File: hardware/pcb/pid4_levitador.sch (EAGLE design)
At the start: 108 parts, among them P1_C1 1u, P1_C2 1u, P1_IC1 TL074CN, P1_IC2 TL074CN, P1_J_IN VSENSOR, P1_J_OUT VPID, P1_J_PWR PWR, P1_POT1 22k, P1_POT2 220k, P1_POT3 22k, P1_R1 10k, P1_R10 1k, P1_R11 1M, P1_R12 160k, P1_R13 240k, P1_R14 96k, P1_R15 160k, P1_R2 10k, P1_R3 10k, P1_R4 10k, P1_R5 10k, P1_R6 1k, P1_R7 10k, P1_R8 10k, P1_R9 10k, P1_RBIAS 4.4k, P1_ROFFSET 10k, P2_C1 1u, P2_C2 1u, P2_IC1 TL074CN, P2_IC2 TL074CN, P2_J_IN VSENSOR, P2_J_OUT VPID, P2_J_PWR PWR, P2_POT1 22k, P2_POT2 220k, P2_POT3 22k, P2_R1 10k, P2_R10 1k, P2_R11 1M, P2_R12 160k, P2_R13 240k, P2_R14 96k, P2_R15 160k, P2_R2 10k, P2_R3 10k, P2_R4 10k, P2_R5 10k, P2_R6 1k, P2_R7 10k, P2_R8 10k, P2_R9 10k, P2_RBIAS 4.4k, P2_ROFFSET 10k, P3_C1 1u, P3_C2 1u, P3_IC1 TL074CN, P3_IC2 TL074CN, P3_J_IN VSENSOR, P3_J_OUT VPID, P3_J_PWR PWR, P3_POT1 22k, P3_POT2 220k, P3_POT3 22k, P3_R1 10k, P3_R10 1k, P3_R11 1M, P3_R12 160k, P3_R13 240k, P3_R14 96k, P3_R15 160k, P3_R2 10k, P3_R3 10k, P3_R4 10k, P3_R5 10k, P3_R6 1k, P3_R7 10k, P3_R8 10k, P3_R9 10k, P3_RBIAS 4.4k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

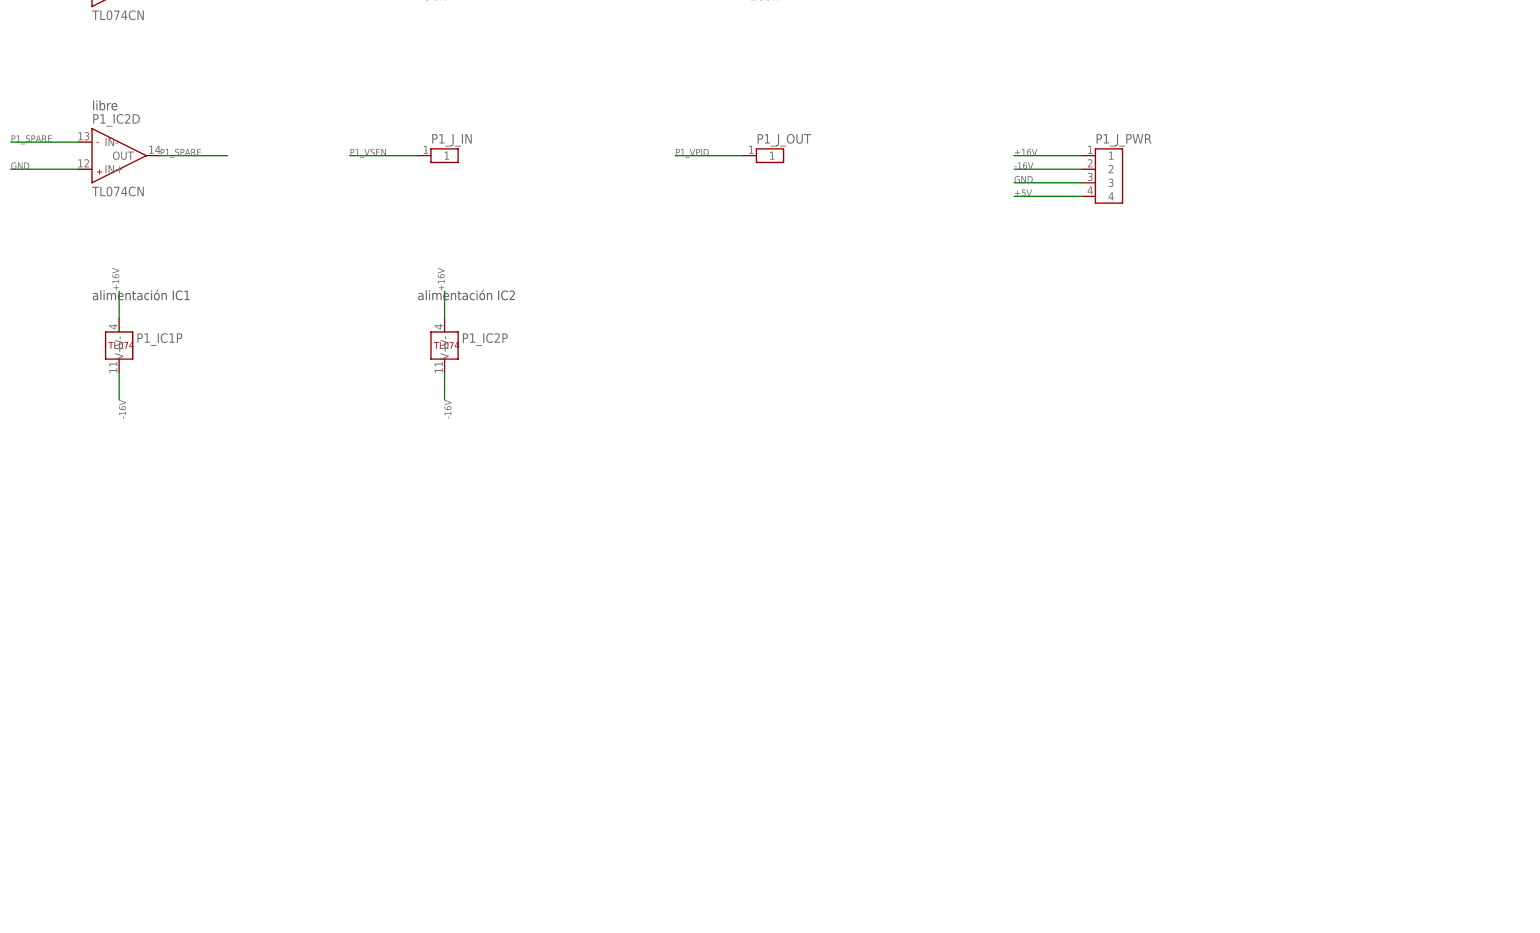
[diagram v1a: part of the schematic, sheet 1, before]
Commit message: Agrega la etapa de potencia a cada uno de los 4 PID de la placa (TIP122, banco de sensado 10 x 1R, protección y bornes de bobina)
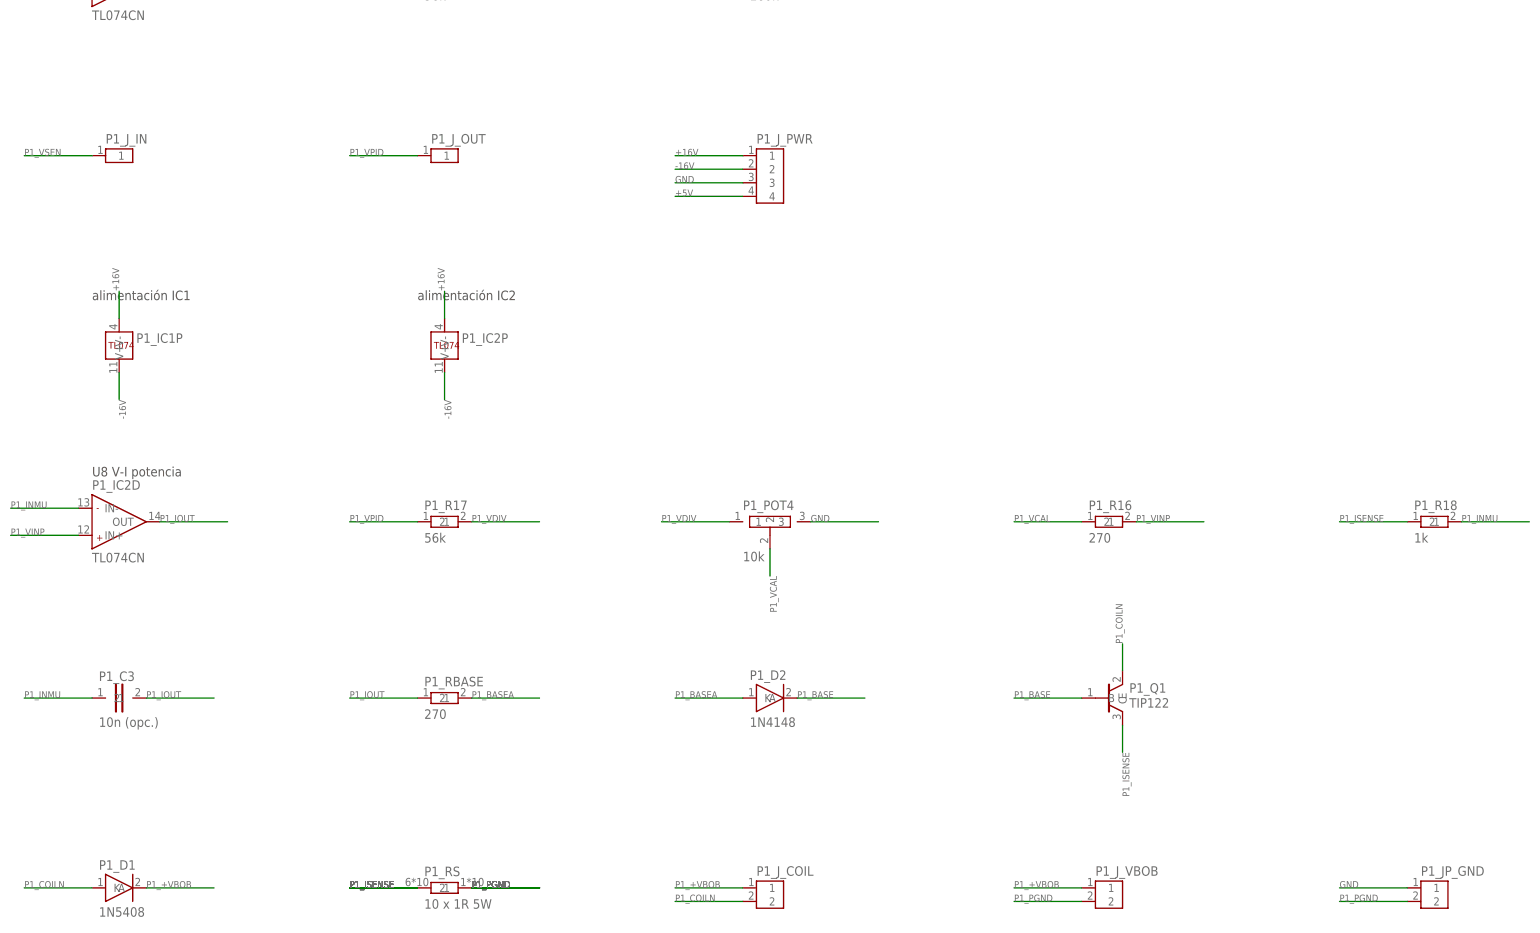
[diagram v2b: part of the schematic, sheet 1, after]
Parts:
- added P1_C3, P2_C3, P3_C3, P4_C3: 10n (opc.), pid4:C
- added P1_D1, P2_D1, P3_D1, P4_D1: 1N5408, pid4:D1N5408
- added P1_D2, P2_D2, P3_D2, P4_D2: 1N4148, pid4:D1N4148
- added P1_JP_GND, P2_JP_GND, P3_JP_GND, P4_JP_GND: GND-PGND, pid4:HDR2
- added P1_J_COIL, P2_J_COIL, P3_J_COIL, P4_J_COIL: BOBINA, pid4:TERM2
- added P1_J_VBOB, P2_J_VBOB, P3_J_VBOB, P4_J_VBOB: VBOB, pid4:TERM2
- added P1_POT4, P2_POT4, P3_POT4, P4_POT4: 10k, pid4:POT
- added P1_Q1, P2_Q1, P3_Q1, P4_Q1: TIP122, pid4:TIP122
- added P1_R16, P1_RBASE, P2_R16, P2_RBASE, P3_R16, P3_RBASE, P4_R16, P4_RBASE: 270, pid4:R
- added P1_R17, P2_R17, P3_R17, P4_R17: 56k, pid4:R
- added P1_R18, P2_R18, P3_R18, P4_R18: 1k, pid4:R
- added P1_RS, P2_RS, P3_RS, P4_RS: 10 x 1R 5W, pid4:RSB
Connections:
- removed net P1_SPARE: P1_IC2D.IN-, P1_IC2D.OUT
- removed net P2_SPARE: P2_IC2D.IN-, P2_IC2D.OUT
- removed net P3_SPARE: P3_IC2D.IN-, P3_IC2D.OUT
- removed net P4_SPARE: P4_IC2D.IN-, P4_IC2D.OUT
- new net P1_+VBOB: P1_D1.K, P1_J_COIL.1, P1_J_VBOB.1
- new net P1_BASE: P1_D2.K, P1_Q1.B
- new net P1_BASEA: P1_D2.A, P1_RBASE.2
- new net P1_COILN: P1_D1.A, P1_J_COIL.2, P1_Q1.C
- new net P1_INMU: P1_C3.1, P1_IC2D.IN-, P1_R18.2
- new net P1_IOUT: P1_C3.2, P1_IC2D.OUT, P1_RBASE.1
- new net P1_ISENSE: P1_Q1.E, P1_R18.1, P1_RS.1
- new net P1_PGND: P1_JP_GND.2, P1_J_VBOB.2, P1_RS.2
- new net P1_VCAL: P1_POT4.2, P1_R16.1
- new net P1_VDIV: P1_POT4.1, P1_R17.2
- new net P1_VINP: P1_IC2D.IN+, P1_R16.2
- new net P2_+VBOB: P2_D1.K, P2_J_COIL.1, P2_J_VBOB.1
- new net P2_BASE: P2_D2.K, P2_Q1.B
- new net P2_BASEA: P2_D2.A, P2_RBASE.2
- new net P2_COILN: P2_D1.A, P2_J_COIL.2, P2_Q1.C
- new net P2_INMU: P2_C3.1, P2_IC2D.IN-, P2_R18.2
- new net P2_IOUT: P2_C3.2, P2_IC2D.OUT, P2_RBASE.1
- new net P2_ISENSE: P2_Q1.E, P2_R18.1, P2_RS.1
- new net P2_PGND: P2_JP_GND.2, P2_J_VBOB.2, P2_RS.2
- new net P2_VCAL: P2_POT4.2, P2_R16.1
- new net P2_VDIV: P2_POT4.1, P2_R17.2
- new net P2_VINP: P2_IC2D.IN+, P2_R16.2
- new net P3_+VBOB: P3_D1.K, P3_J_COIL.1, P3_J_VBOB.1
- new net P3_BASE: P3_D2.K, P3_Q1.B
- new net P3_BASEA: P3_D2.A, P3_RBASE.2
- new net P3_COILN: P3_D1.A, P3_J_COIL.2, P3_Q1.C
- new net P3_INMU: P3_C3.1, P3_IC2D.IN-, P3_R18.2
- new net P3_IOUT: P3_C3.2, P3_IC2D.OUT, P3_RBASE.1
- new net P3_ISENSE: P3_Q1.E, P3_R18.1, P3_RS.1
- new net P3_PGND: P3_JP_GND.2, P3_J_VBOB.2, P3_RS.2
- new net P3_VCAL: P3_POT4.2, P3_R16.1
- new net P3_VDIV: P3_POT4.1, P3_R17.2
- new net P3_VINP: P3_IC2D.IN+, P3_R16.2
- new net P4_+VBOB: P4_D1.K, P4_J_COIL.1, P4_J_VBOB.1
- new net P4_BASE: P4_D2.K, P4_Q1.B
- new net P4_BASEA: P4_D2.A, P4_RBASE.2
- new net P4_COILN: P4_D1.A, P4_J_COIL.2, P4_Q1.C
- new net P4_INMU: P4_C3.1, P4_IC2D.IN-, P4_R18.2
- new net P4_IOUT: P4_C3.2, P4_IC2D.OUT, P4_RBASE.1
- new net P4_ISENSE: P4_Q1.E, P4_R18.1, P4_RS.1
- new net P4_PGND: P4_JP_GND.2, P4_J_VBOB.2, P4_RS.2
- new net P4_VCAL: P4_POT4.2, P4_R16.1
- new net P4_VDIV: P4_POT4.1, P4_R17.2
- new net P4_VINP: P4_IC2D.IN+, P4_R16.2
- net GND: now also P1_JP_GND.1, P1_POT4.3, P2_JP_GND.1, P2_POT4.3, P3_JP_GND.1, P3_POT4.3, P4_JP_GND.1, P4_POT4.3; no longer P1_IC2D.IN+, P2_IC2D.IN+, P3_IC2D.IN+, P4_IC2D.IN+
- net P1_VPID: now also P1_R17.1
- net P2_VPID: now also P2_R17.1
- net P3_VPID: now also P3_R17.1
- net P4_VPID: now also P4_R17.1
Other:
- note added: "U8 V-I potencia"
- note removed: "libre"
- moved on the sheet: P1_IC2D, P1_J_IN, P1_J_OUT, P1_J_PWR, P2_IC2D, P2_J_IN, P2_J_OUT, P2_J_PWR, P3_IC2D, P3_J_IN, P3_J_OUT, P3_J_PWR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
